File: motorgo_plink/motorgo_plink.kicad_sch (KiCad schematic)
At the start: 21 parts, among them J1 USB4520-03-0-A_REVA, J4 Conn_02x20_Odd_Even, U1 ESP32-S3-WROOM-1, U2 USBLC6-2P6

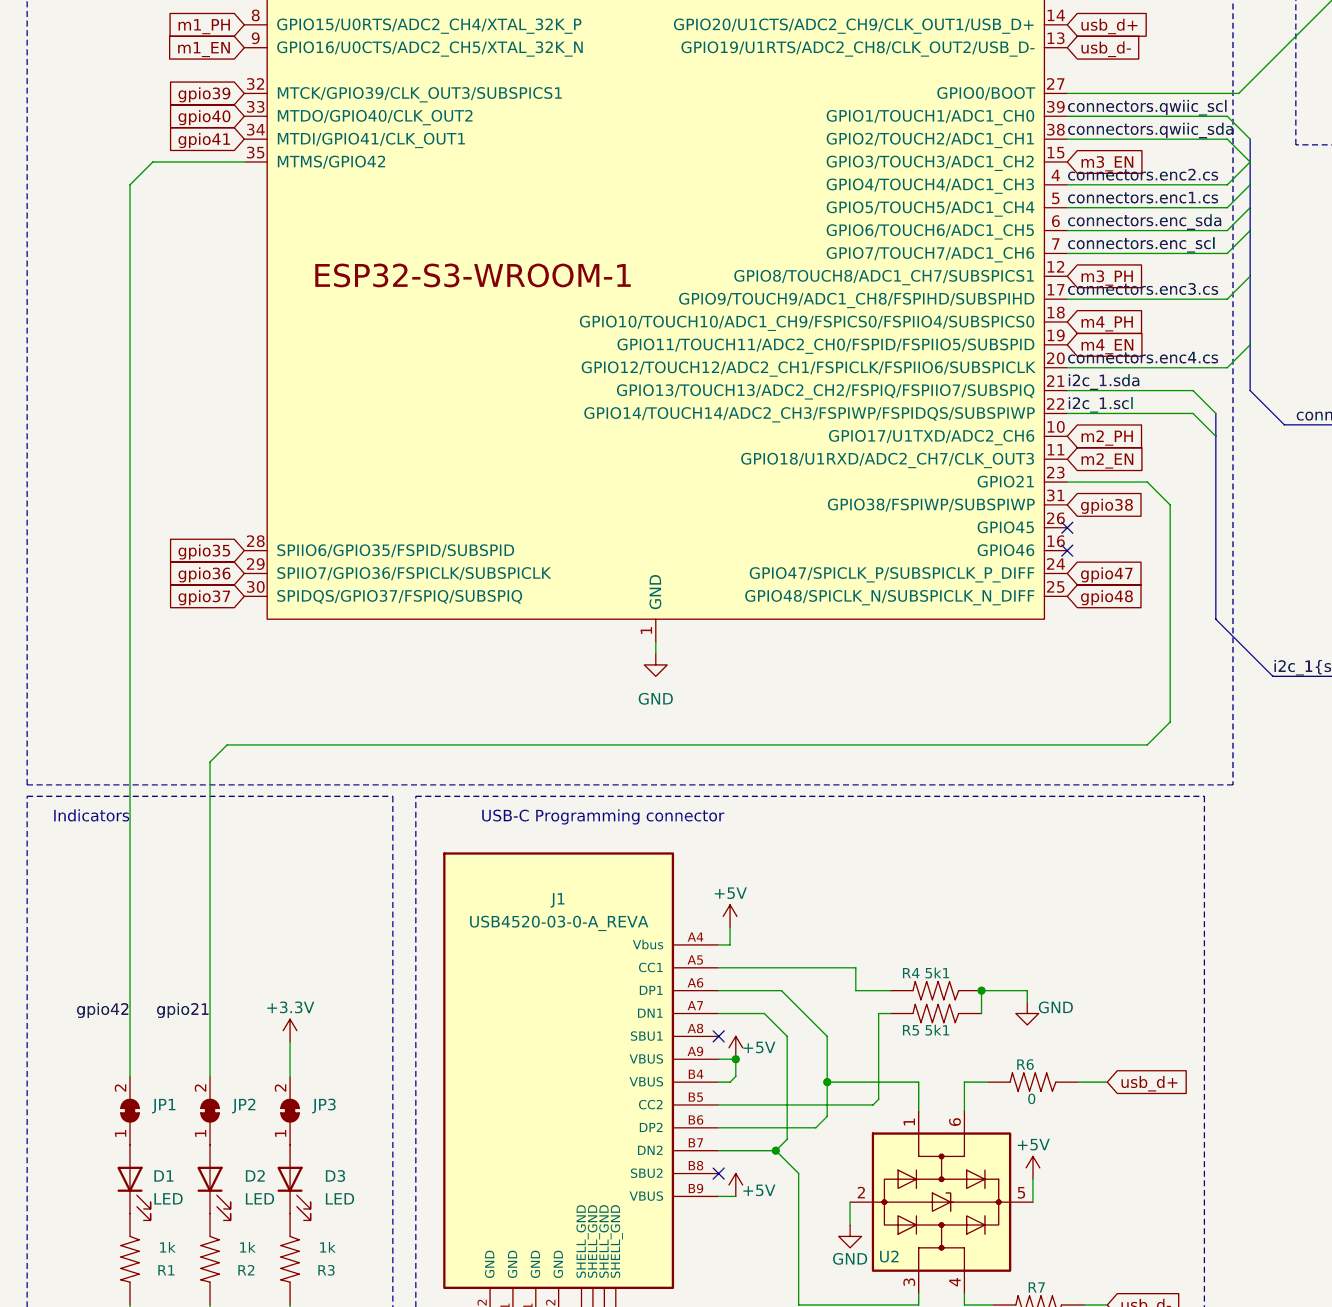
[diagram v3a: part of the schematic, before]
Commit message: wip layout work begun, board dimensions finalized
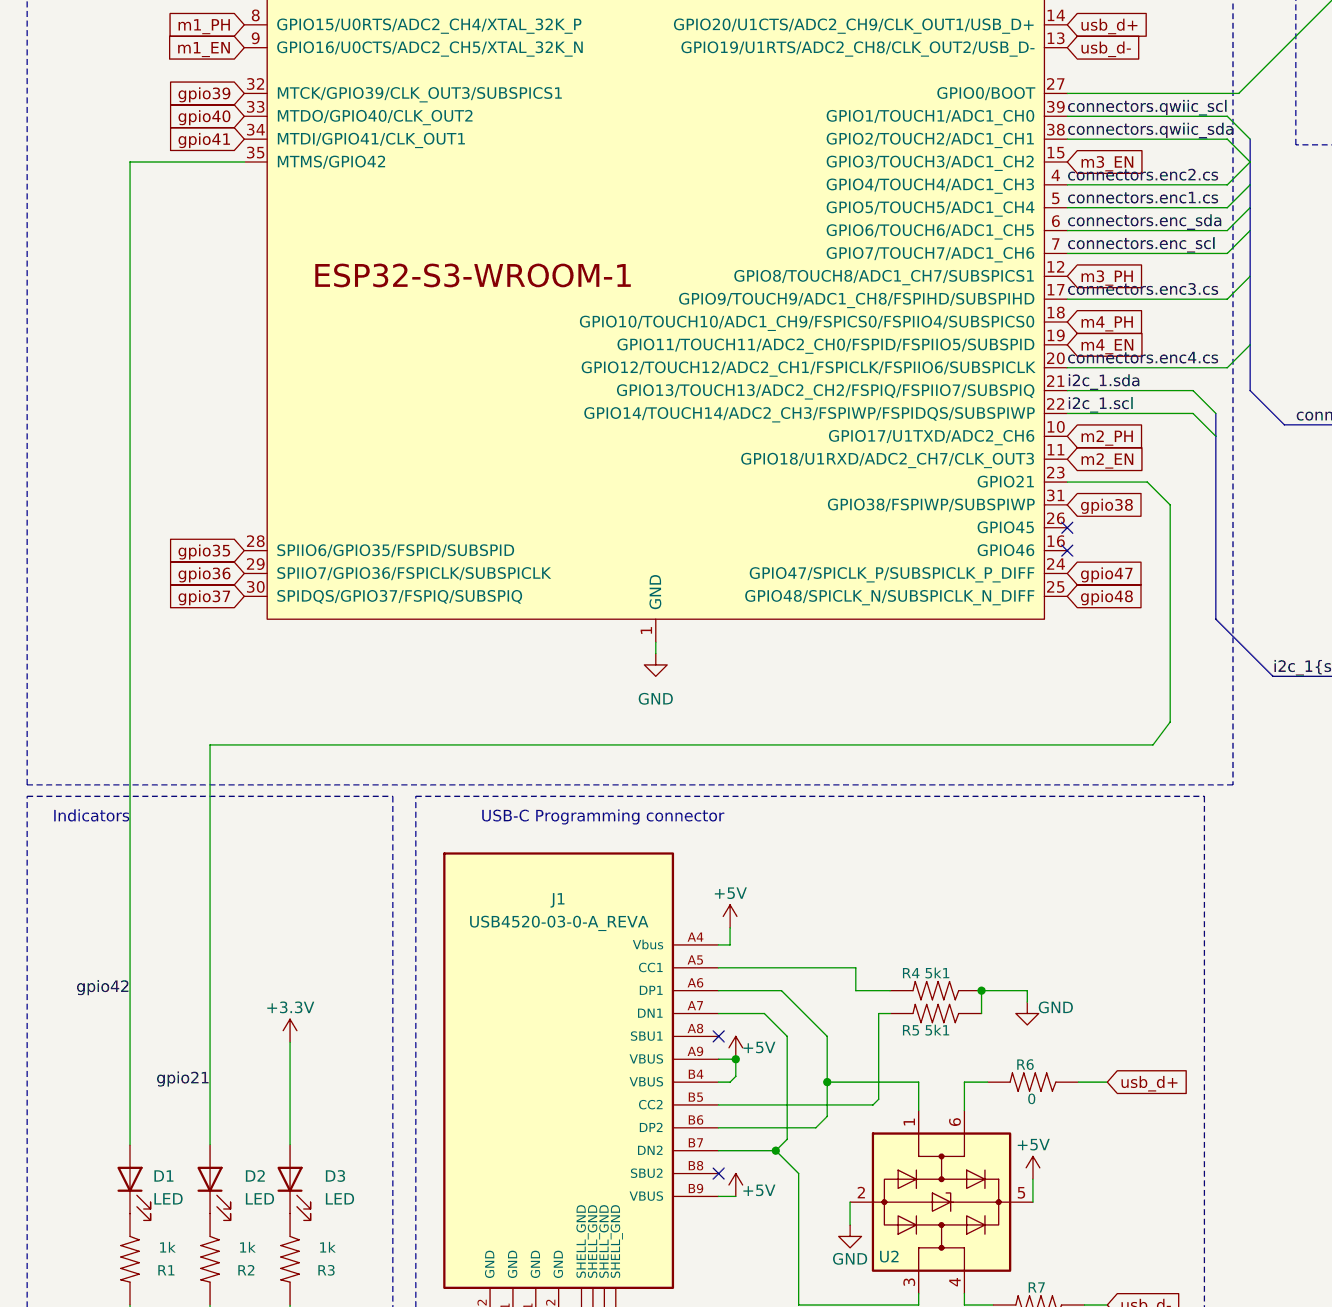
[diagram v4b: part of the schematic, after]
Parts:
- removed JP1, JP2, JP3: DNP, Jumper:SolderJumper-2_P1.3mm_Open_RoundedPad1.0x1.5mm, symbol Jumper:SolderJumper_2_Bridged
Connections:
- net +3.3V: now also D3.2 (A)
- net gpio21: now also D2.2 (A)
- net gpio42: now also D1.2 (A)

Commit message: layout complete! checkpoint ready for design review
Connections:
- net gpio3 is gone; now on net reset: J4.16 (Pin_16)
- net gpio4 is gone; now on net gpio39: J4.12 (Pin_12)
- net gpio7 is gone; now on net GND: J4.13 (Pin_13)
- net gpio8 is gone; now on net +3.3V: J4.18 (Pin_18)
- net gpio9 is gone; now on net gpio43: J4.7 (Pin_7)
- net +3.3V: now also J4.2 (Pin_2); no longer J4.1 (Pin_1), J4.17 (Pin_17)
- net +5V: now also J4.1 (Pin_1), J4.3 (Pin_3); no longer J4.2 (Pin_2), J4.4 (Pin_4)
- net GND: now also J4.10 (Pin_10), J4.19 (Pin_19), J4.26 (Pin_26), J4.29 (Pin_29), J4.33 (Pin_33), J4.40 (Pin_40), J4.5 (Pin_5); no longer J4.14 (Pin_14), J4.20 (Pin_20), J4.25 (Pin_25), J4.30 (Pin_30), J4.34 (Pin_34), J4.39 (Pin_39), J4.6 (Pin_6), J4.9 (Pin_9)
- net connectors.enc1.cs: now also U1.4 (GPIO4/TOUCH4/ADC1_CH3); no longer U1.5 (GPIO5/TOUCH5/ADC1_CH4)
- net connectors.enc2.cs: now also U1.5 (GPIO5/TOUCH5/ADC1_CH4); no longer U1.4 (GPIO4/TOUCH4/ADC1_CH3)
- net connectors.enc3.cs: now also U1.18 (GPIO10/TOUCH10/ADC1_CH9/FSPICS0/FSPIIO4/SUBSPICS0); no longer U1.17 (GPIO9/TOUCH9/ADC1_CH8/FSPIHD/SUBSPIHD)
- net connectors.enc4.cs: now also U1.17 (GPIO9/TOUCH9/ADC1_CH8/FSPIHD/SUBSPIHD); no longer U1.20 (GPIO12/TOUCH12/ADC2_CH1/FSPICLK/FSPIIO6/SUBSPICLK)
- net connectors.qwiic_scl: now also U1.38 (GPIO2/TOUCH2/ADC1_CH1); no longer U1.39 (GPIO1/TOUCH1/ADC1_CH0)
- net connectors.qwiic_sda: now also U1.39 (GPIO1/TOUCH1/ADC1_CH0); no longer U1.38 (GPIO2/TOUCH2/ADC1_CH1)
- net gpio21: now also J4.23 (Pin_23); no longer D2.2 (A)
- net gpio35: now also J4.20 (Pin_20)
- net gpio36: now also J4.21 (Pin_21)
- net gpio37: now also J4.14 (Pin_14)
- net gpio38: now also J4.17 (Pin_17); no longer J4.24 (Pin_24)
- net gpio39: no longer J4.21 (Pin_21)
- net gpio40: now also J4.15 (Pin_15); no longer J4.23 (Pin_23)
- net gpio41: now also J4.11 (Pin_11); no longer J4.22 (Pin_22)
- net gpio42: now also J4.9 (Pin_9); no longer D1.2 (A), J4.19 (Pin_19)
- net gpio43: now also D2.2 (A); no longer J4.8 (Pin_8)
- net gpio44: now also D1.2 (A), J4.8 (Pin_8); no longer J4.10 (Pin_10)
- net gpio47: now also J4.24 (Pin_24); no longer J4.11 (Pin_11)
- net gpio48: now also J4.22 (Pin_22)
- net m2_EN: now also U1.10 (GPIO17/U1TXD/ADC2_CH6); no longer U1.11 (GPIO18/U1RXD/ADC2_CH7/CLK_OUT3)
- net m2_PH: now also U1.11 (GPIO18/U1RXD/ADC2_CH7/CLK_OUT3); no longer U1.10 (GPIO17/U1TXD/ADC2_CH6)
- net m3_EN: now also U1.12 (GPIO8/TOUCH8/ADC1_CH7/SUBSPICS1); no longer U1.15 (GPIO3/TOUCH3/ADC1_CH2)
- net m3_PH: now also U1.15 (GPIO3/TOUCH3/ADC1_CH2); no longer U1.12 (GPIO8/TOUCH8/ADC1_CH7/SUBSPICS1)
- net m4_PH: now also U1.20 (GPIO12/TOUCH12/ADC2_CH1/FSPICLK/FSPIIO6/SUBSPICLK); no longer U1.18 (GPIO10/TOUCH10/ADC1_CH9/FSPICS0/FSPIIO4/SUBSPICS0)
- net p26: now also J4.25 (Pin_25); no longer J4.26 (Pin_26)
- net p31: now also J4.32 (Pin_32); no longer J4.31 (Pin_31)
- net p32: now also J4.31 (Pin_31); no longer J4.32 (Pin_32)
- net p33: now also J4.34 (Pin_34); no longer J4.33 (Pin_33)
- net p35: now also J4.36 (Pin_36); no longer J4.35 (Pin_35)
- net p36: now also J4.35 (Pin_35); no longer J4.36 (Pin_36)
- net p37: now also J4.38 (Pin_38); no longer J4.37 (Pin_37)
- net p38: now also J4.37 (Pin_37); no longer J4.38 (Pin_38)
- net p40: now also J4.39 (Pin_39); no longer J4.40 (Pin_40)
- net reset: no longer J4.15 (Pin_15)
- net scl: now also J4.6 (Pin_6); no longer J4.5 (Pin_5)
- net sda: now also J4.4 (Pin_4); no longer J4.3 (Pin_3)
- net Boot renamed boot
- net boot: now also J4.30 (Pin_30); no longer J4.29 (Pin_29)
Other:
- sheet IMU 6 + 3 ports: added SCL, SDA; removed scl_imu, sda_imu

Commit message: production files and all edits for final send off of v1.0
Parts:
- R1, R2, R3: LCSC_Part_Number C2906899 -> C11702
- R4, R5, R8, R9: LCSC_Part_Number C409700 -> C25905
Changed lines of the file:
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@@
 	(label "connectors.enc1.cs"
 		(at 129.54 55.88 0)
+		(fields_autoplaced yes)
 		(effects
 			(font
@@
 	(label "connectors.enc2.cs"
 		(at 129.54 58.42 0)
+		(fields_autoplaced yes)
 		(effects
 			(font
@@
 			)
 		)
-		(property "LCSC_Part_Number" "C409700"
+		(property "LCSC_Part_Number" "C25905"
 			(at 114.935 147.955 0)
 			(effects
@@
 			)
 		)
-		(property "LCSC_Part_Number" "C409700"
+		(property "LCSC_Part_Number" "C25905"
 			(at 167.64 29.21 0)
 			(effects
@@
 			)
 		)
-		(property "LCSC_Part_Number" "C409700"
+		(property "LCSC_Part_Number" "C25905"
 			(at 183.515 29.21 0)
 			(effects
@@
 			)
 		)
-		(property "LCSC_Part_Number" "C2906899"
+		(property "LCSC_Part_Number" "C11702"
 			(at 25.4 175.26 0)
 			(effects
@@
 			)
 		)
-		(property "LCSC_Part_Number" "C2906899"
+		(property "LCSC_Part_Number" "C11702"
 			(at 43.18 175.26 0)
 			(effects
@@
 			)
 		)
-		(property "LCSC_Part_Number" "C409700"
+		(property "LCSC_Part_Number" "C25905"
 			(at 114.935 145.415 0)
 			(effects
@@
 			)
 		)
-		(property "LCSC_Part_Number" "C2906899"
+		(property "LCSC_Part_Number" "C11702"
 			(at 34.29 175.26 0)
 			(effects

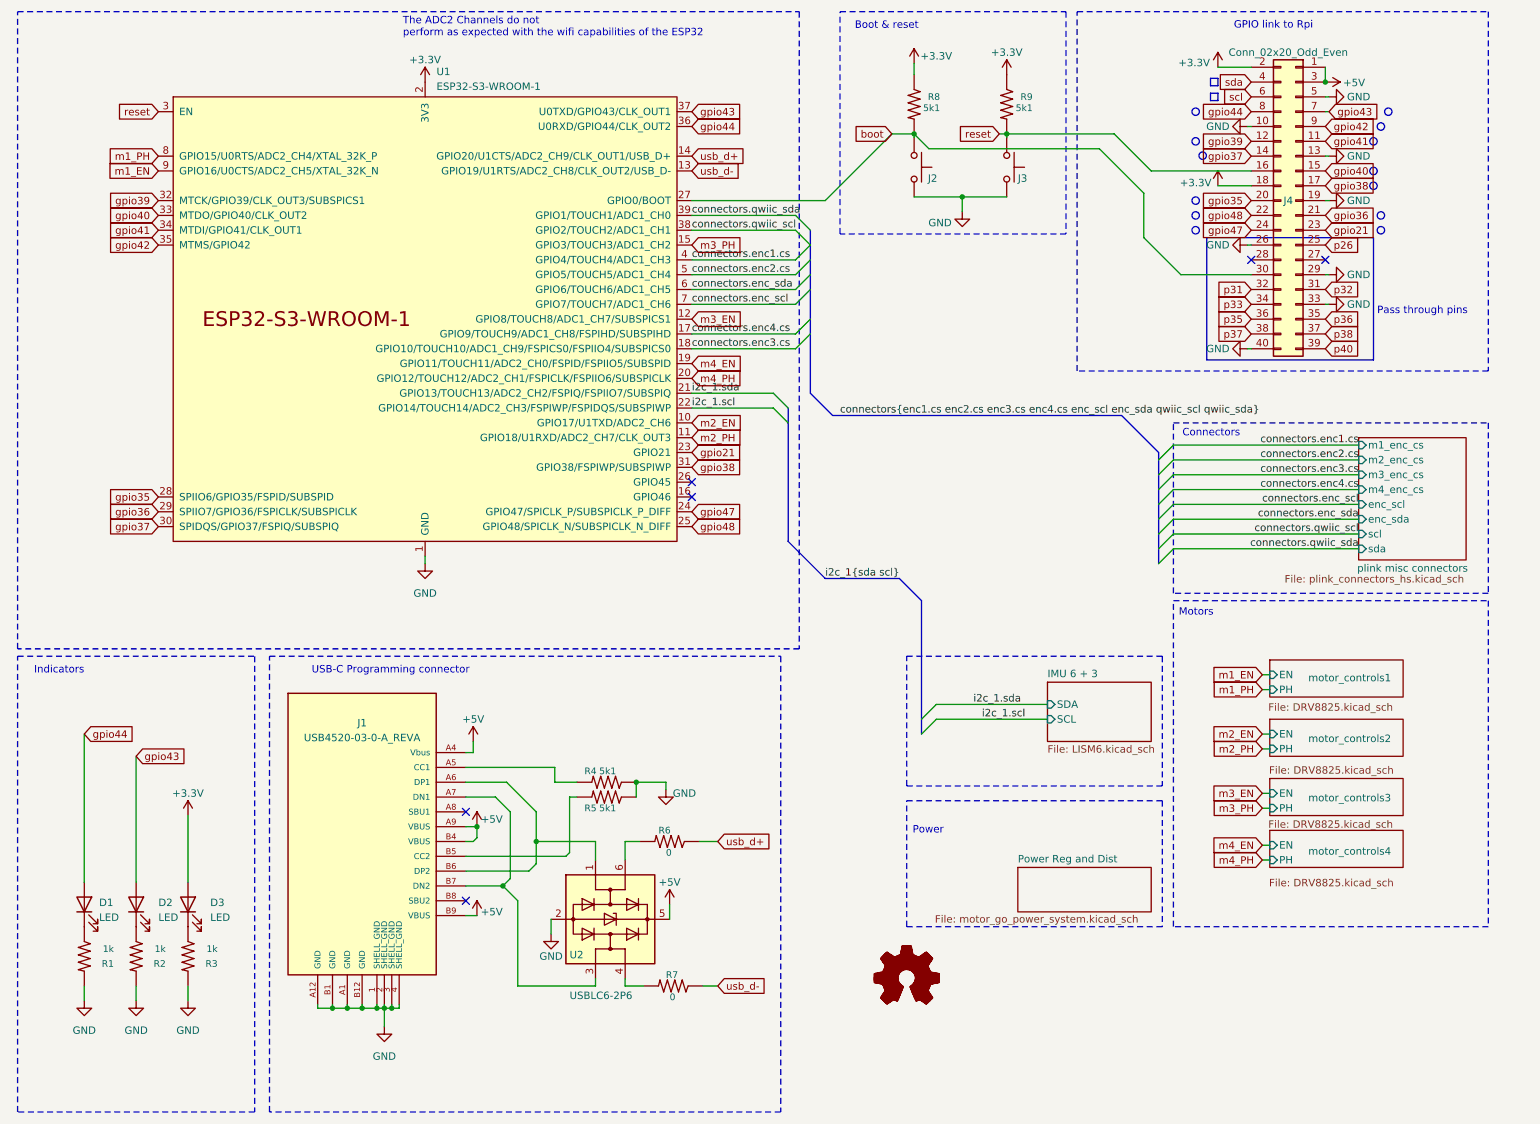
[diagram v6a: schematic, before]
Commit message: updated schematic to fix IMU i2c mismatch, silkscreen readability, schottky backpower diode, and added RC Servo pins
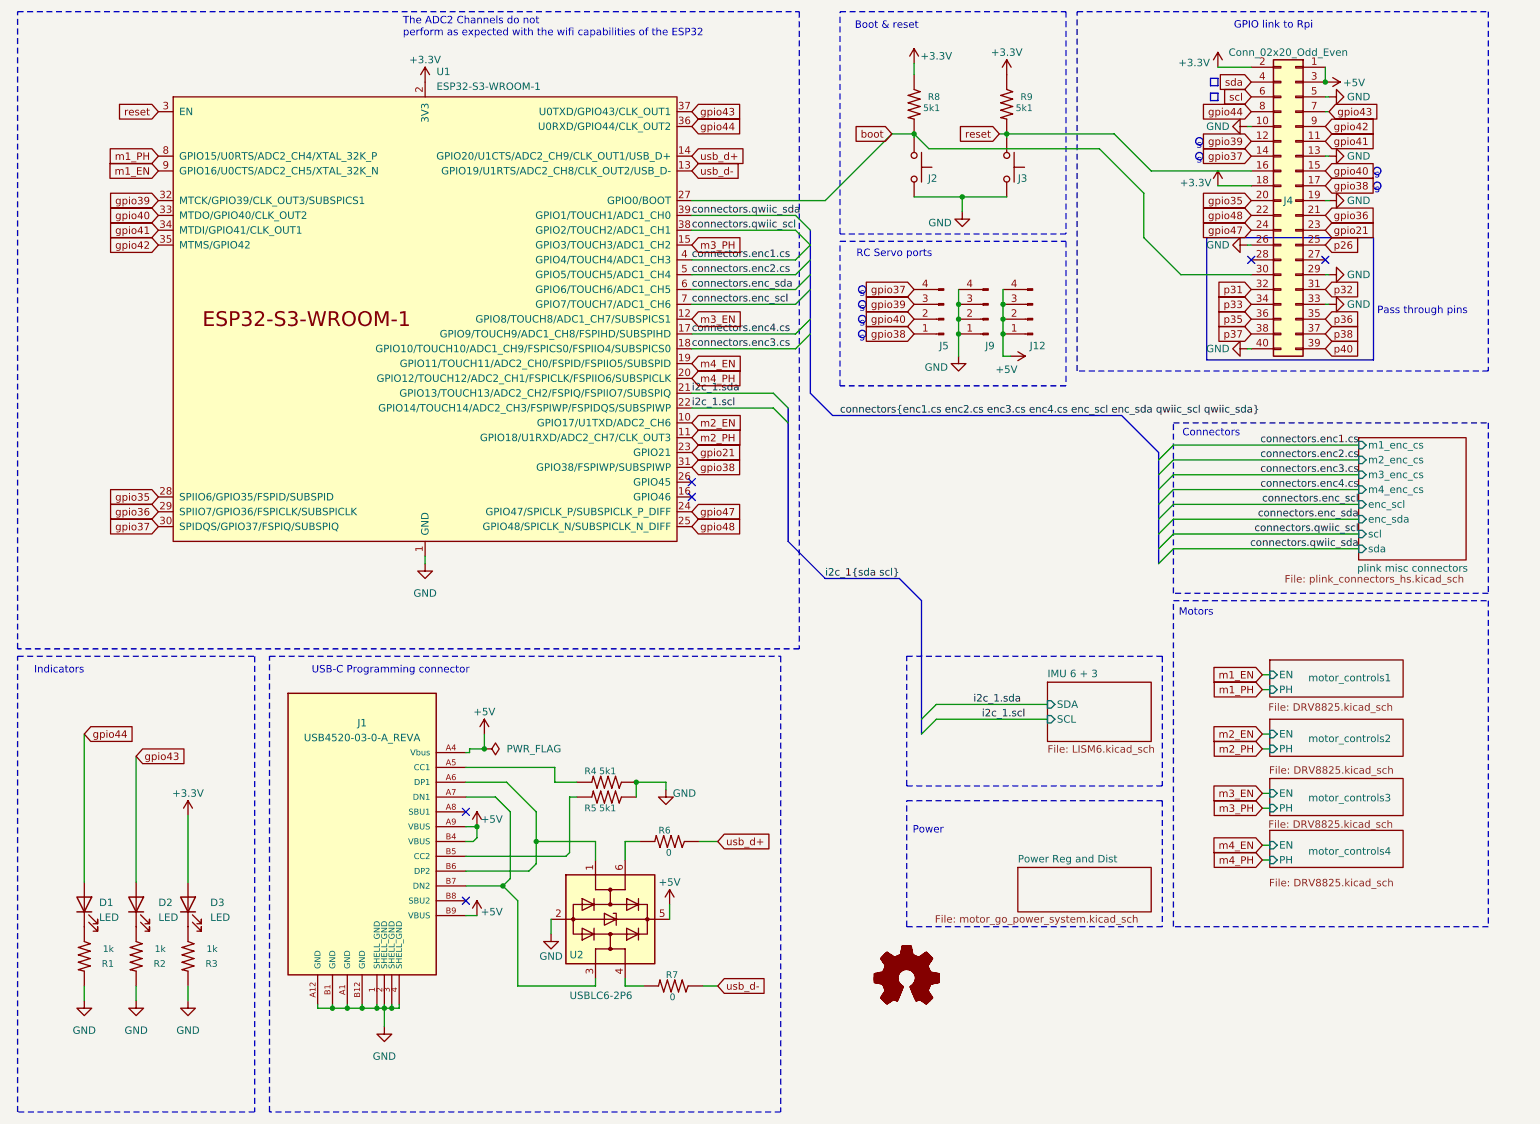
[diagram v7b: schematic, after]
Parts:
- added J12, J5, J9: Conn_01x04_Pin, Connector_PinHeader_2.54mm:PinHeader_1x04_P2.54mm_Vertical, symbol Connector:Conn_01x04_Pin
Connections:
- net +5V: now also J12.1 (Pin_1), J12.2 (Pin_2), J12.3 (Pin_3), J12.4 (Pin_4)
- net GND: now also J9.1 (Pin_1), J9.2 (Pin_2), J9.3 (Pin_3), J9.4 (Pin_4)
- net gpio37: now also J5.4 (Pin_4)
- net gpio38: now also J5.1 (Pin_1)
- net gpio39: now also J5.3 (Pin_3)
- net gpio40: now also J5.2 (Pin_2)
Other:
- note added: "RC Servo ports"
- note added: "s"
